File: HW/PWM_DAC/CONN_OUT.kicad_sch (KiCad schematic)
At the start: 1 part, among them J502 1715721

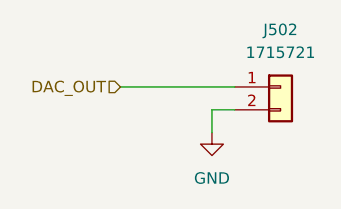
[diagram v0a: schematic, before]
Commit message: Schematic done
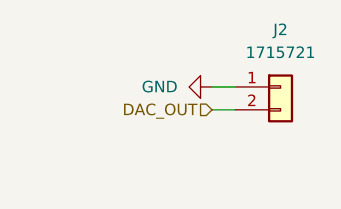
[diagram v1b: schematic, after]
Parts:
- renumbered J502 to J2
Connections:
- net DAC_OUT: now also J2.2 (Pin_2); no longer J2.1 (Pin_1)
- net GND: now also J2.1 (Pin_1); no longer J2.2 (Pin_2)
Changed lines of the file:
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@@
+	(wire
+		(pts
+			(xy 196.85 115.57) (xy 199.39 115.57)
+		)
+		(stroke
+			(width 0)
+			(type default)
+		)
+	)
 	(wire
 		(pts
@@
 		)
 	)
-	(wire
-		(pts
-			(xy 196.85 120.65) (xy 196.85 118.11)
-		)
-		(stroke
-			(width 0)
-			(type default)
-		)
-	)
-	(wire
-		(pts
-			(xy 186.69 115.57) (xy 199.39 115.57)
-		)
-		(stroke
-			(width 0)
-			(type default)
-		)
-	)
 	(hierarchical_label "DAC_OUT"
 		(shape input)
-		(at 186.69 115.57 180)
+		(at 196.85 118.11 180)
 		(effects
 			(font
@@
 	(symbol
 		(lib_id "power:GND")
-		(at 196.85 120.65 0)
+		(at 196.85 115.57 270)
 		(unit 1)
 		(body_style 1)
@@
 		(dnp no)
 		(fields_autoplaced yes)
-		(property "Reference" "#PWR038"
-			(at 196.85 127 0)
+		(property "Reference" "#PWR094"
+			(at 190.5 115.57 0)
 			(hide yes)
 			(show_name no)
@@
 		)
 		(property "Value" "GND"
-			(at 196.85 125.73 0)
+			(at 193.04 115.5699 90)
 			(show_name no)
 			(do_not_autoplace no)
@@
 					(size 1.27 1.27)
 				)
+				(justify right)
 			)
 		)
 		(property "Footprint" ""
-			(at 196.85 120.65 0)
+			(at 196.85 115.57 0)
 			(hide yes)
 			(show_name no)
@@
 		)
 		(property "Datasheet" ""
-			(at 196.85 120.65 0)
+			(at 196.85 115.57 0)
 			(hide yes)
 			(show_name no)
@@
 		)
 		(property "Description" "Power symbol creates a global label with name \"GND\" , ground"
-			(at 196.85 120.65 0)
+			(at 196.85 115.57 0)
 			(hide yes)
 			(show_name no)
@@
 			(project "PWM_DAC"
 				(path "/2c9a3dd6-931b-4123-b00f-9baea7dc6b77/dcf01361-02cc-4d84-89bc-3e429e190ed8"
-					(reference "#PWR038")
+					(reference "#PWR094")
 					(unit 1)
 				)
@@
 		(in_pos_files yes)
 		(dnp no)
-		(property "Reference" "J502"
+		(property "Reference" "J2"
 			(at 204.47 109.22 0)
 			(show_name no)
@@
 			(project "PWM_DAC"
 				(path "/2c9a3dd6-931b-4123-b00f-9baea7dc6b77/dcf01361-02cc-4d84-89bc-3e429e190ed8"
-					(reference "J502")
+					(reference "J2")
 					(unit 1)
 				)

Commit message: Layout done
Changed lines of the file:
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@@
 	(wire
 		(pts
-			(xy 196.85 118.11) (xy 199.39 118.11)
+			(xy 193.04 118.11) (xy 199.39 118.11)
 		)
 		(stroke
@@
 	(hierarchical_label "DAC_OUT"
 		(shape input)
-		(at 196.85 118.11 180)
+		(at 193.04 118.11 180)
 		(effects
 			(font
@@
 			)
 			(justify right)
+		)
+	)
+	(rule_area
+		(exclude_from_sim no)
+		(in_bom yes)
+		(on_board yes)
+		(dnp no)
+		(polyline
+			(pts
+				(xy 13.97 16.51) (xy 406.4 16.51) (xy 406.4 251.46) (xy 298.45 251.46) (xy 298.45 283.21) (xy 13.97 283.21)
+			)
+			(stroke
+				(width 0)
+				(type dash)
+			)
+			(fill
+				(type none)
+			)
+		)
+	)
+	(netclass_flag ""
+		(length 2.54)
+		(shape round)
+		(at 13.97 16.51 0)
+		(fields_autoplaced yes)
+		(effects
+			(font
+				(size 1.27 1.27)
+			)
+			(justify left bottom)
+		)
+		(property "Netclass" "GND"
+			(at 14.6685 13.97 0)
+			(show_name no)
+			(do_not_autoplace no)
+			(effects
+				(font
+					(size 1.27 1.27)
+				)
+				(justify left)
+			)
+		)
+		(property "Component Class" ""
+			(at -640.08 -81.28 0)
+			(show_name no)
+			(do_not_autoplace no)
+			(effects
+				(font
+					(size 1.27 1.27)
+					(italic yes)
+				)
+			)
 		)
 	)
@@
 		(dnp no)
 		(fields_autoplaced yes)
-		(property "Reference" "#PWR094"
+		(property "Reference" "#PWR093"
 			(at 190.5 115.57 0)
 			(hide yes)
@@
 			(project "PWM_DAC"
 				(path "/2c9a3dd6-931b-4123-b00f-9baea7dc6b77/dcf01361-02cc-4d84-89bc-3e429e190ed8"
-					(reference "#PWR094")
+					(reference "#PWR093")
 					(unit 1)
 				)
@@
 			(at 204.47 115.57 0)
 			(hide yes)
+			(show_name no)
+			(do_not_autoplace no)
+			(effects
+				(font
+					(size 1.27 1.27)
+				)
+			)
+		)
+		(property "Sim.Device" ""
+			(at 204.47 115.57 0)
+			(hide yes)
+			(show_name no)
+			(do_not_autoplace no)
+			(effects
+				(font
+					(size 1.27 1.27)
+				)
+			)
+		)
+		(property "Sim.Pins" ""
+			(at 204.47 115.57 0)
+			(hide yes)
